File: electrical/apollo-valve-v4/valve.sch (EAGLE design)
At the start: 83 parts, among them J1 VALVE2, J2 VALVE1, J4 S1, J5 S2, U1 DRV8806-SSOP, U2 DRV8806-SSOP, U3 TPS54202, U4 DRV8806-SSOP, U5 DRV8806-SSOP, U6 TPS54202

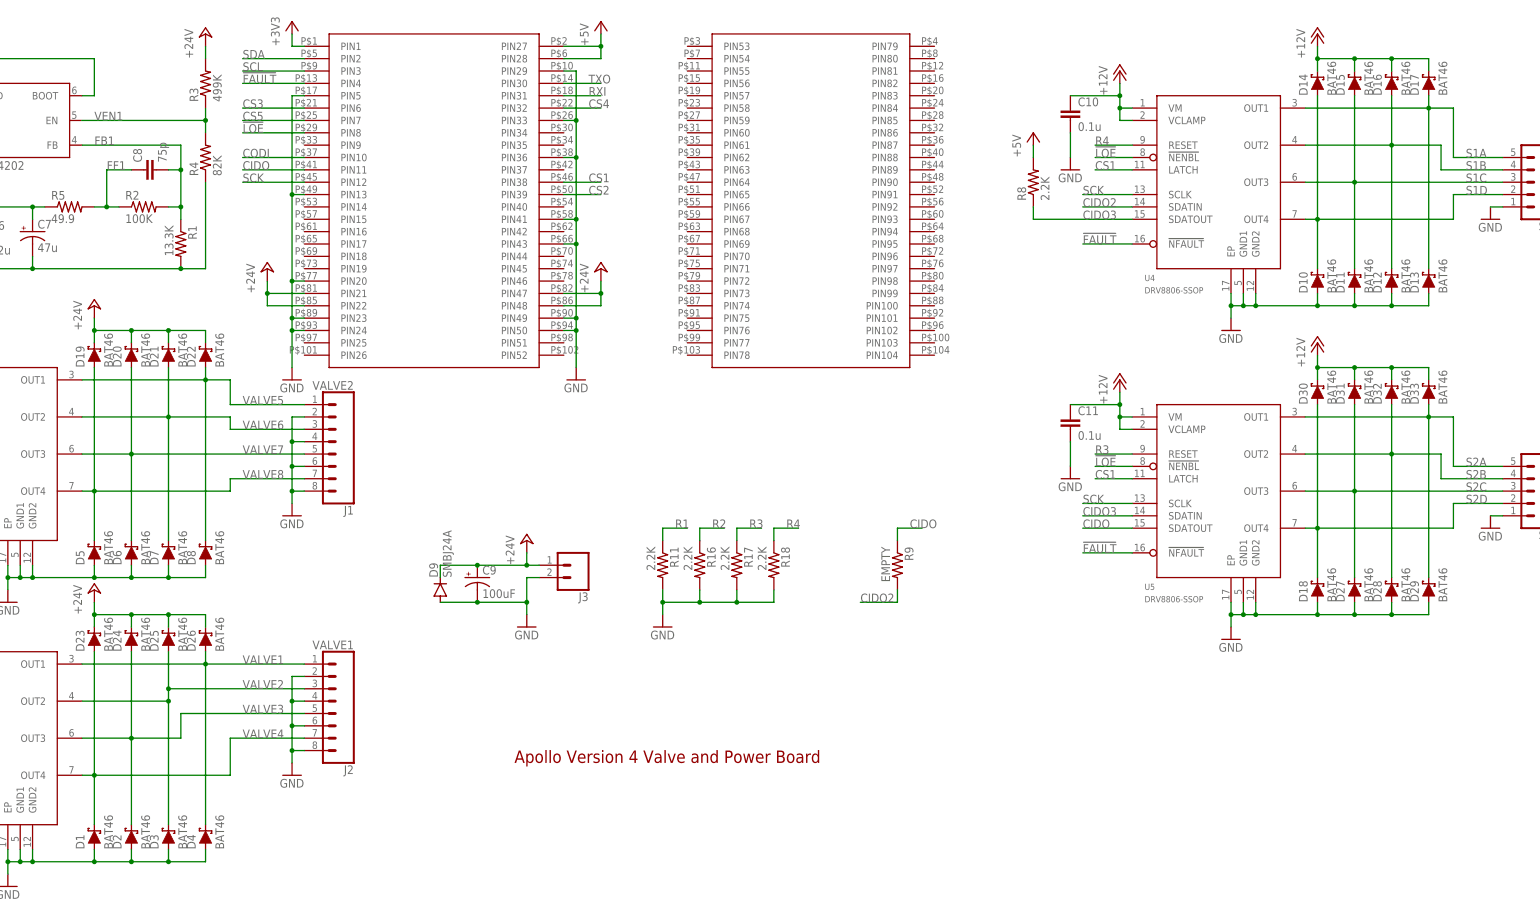
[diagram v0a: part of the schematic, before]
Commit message: Clean up valve board silkscreen and change diodes to SOD-123
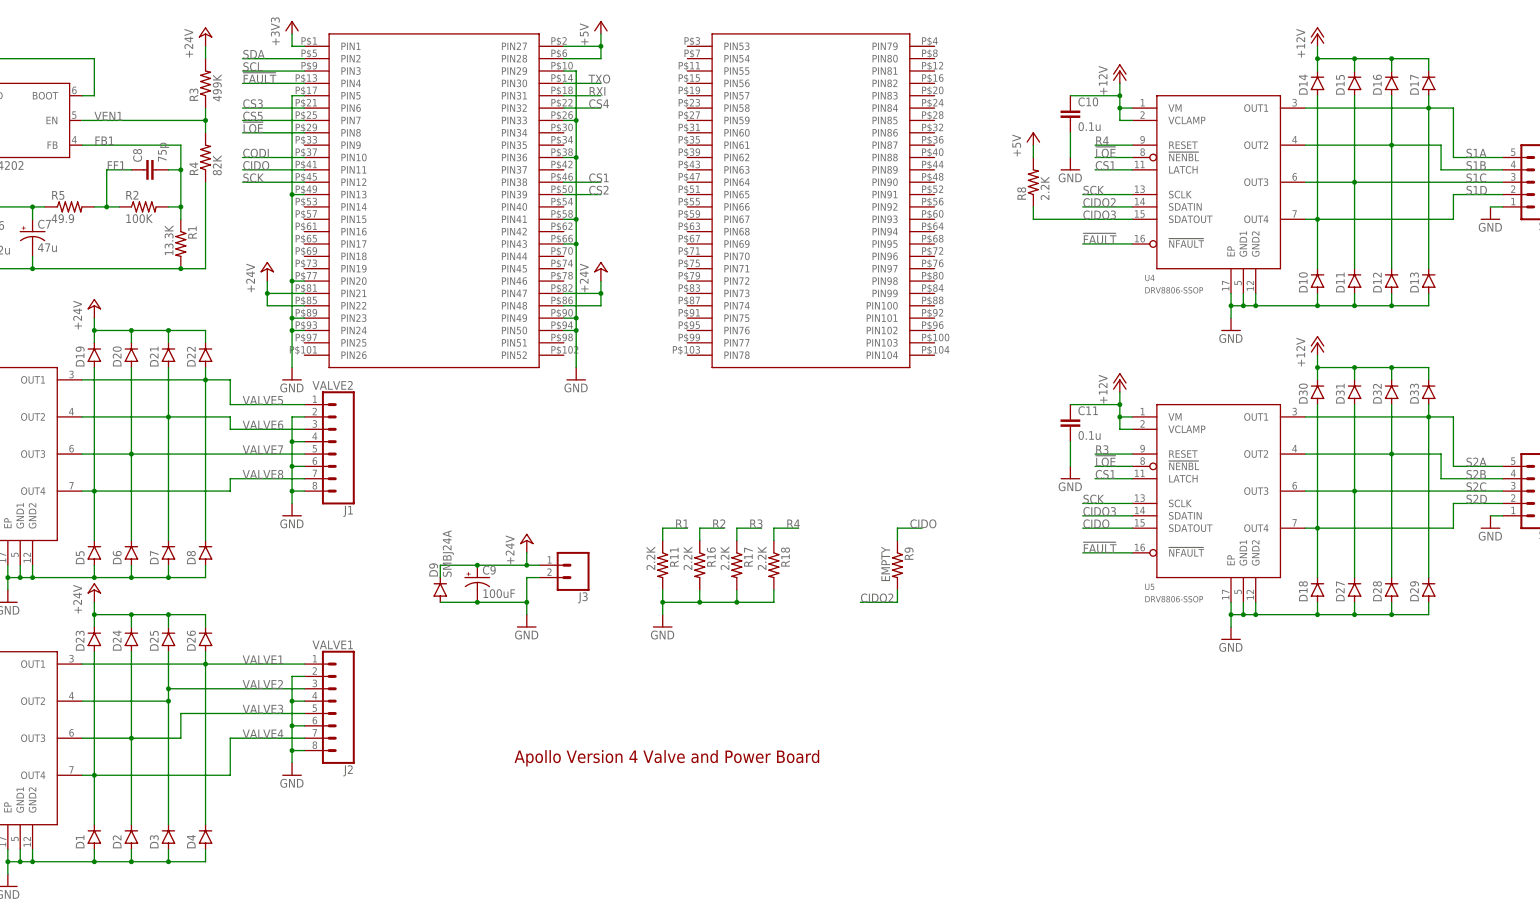
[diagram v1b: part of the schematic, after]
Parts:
- D1, D10, D11, D12, D13, D14, D15, D16, D17, D18, D19, D2, D20, D21, D22, D23, D24, D25, D26, D27, D28, D29, D3, D30, D31, D32, D33, D4, D5, D6, D7, D8: value BAT46 -> B5819W; device SparkFun-DiscreteSemi:DIODE-SCHOTTKY-BAT60A -> diode:DIODE-SOD123
